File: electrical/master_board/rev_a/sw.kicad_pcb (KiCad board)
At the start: 2 copper layers, 66.2 x 45.2 mm, 7 parts, among them CN108 BRIDGE_SW_OUTER;M1x8

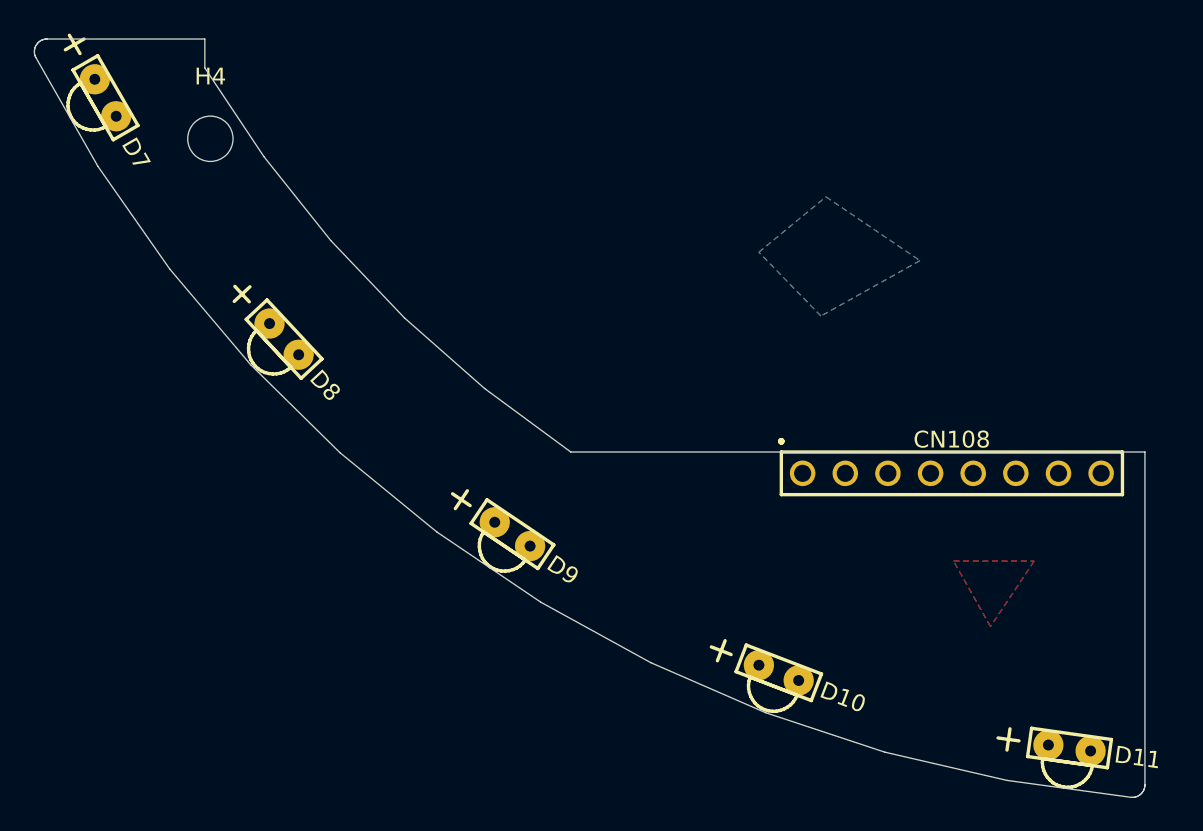
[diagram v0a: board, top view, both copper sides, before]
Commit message: The four corner boards ne/nw/se/sw are now zoned.
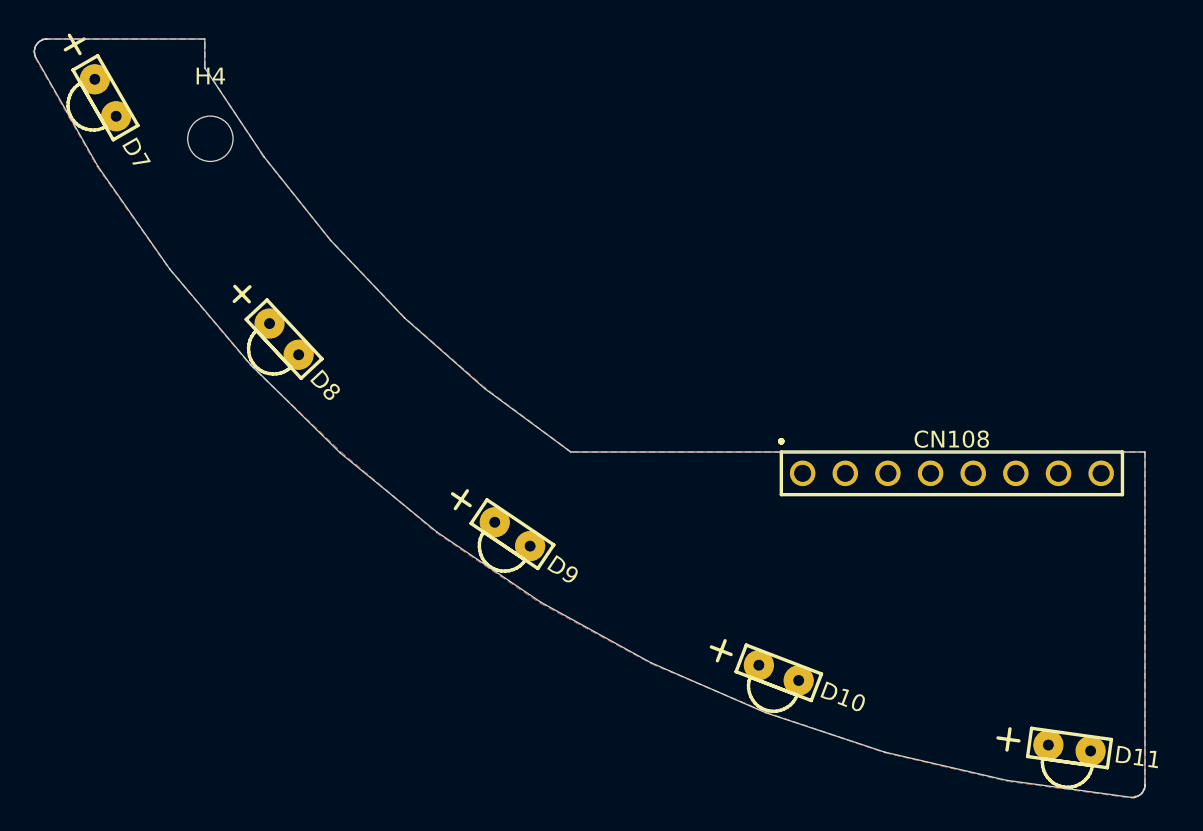
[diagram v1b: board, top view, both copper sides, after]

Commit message: Layed out SW PCB.
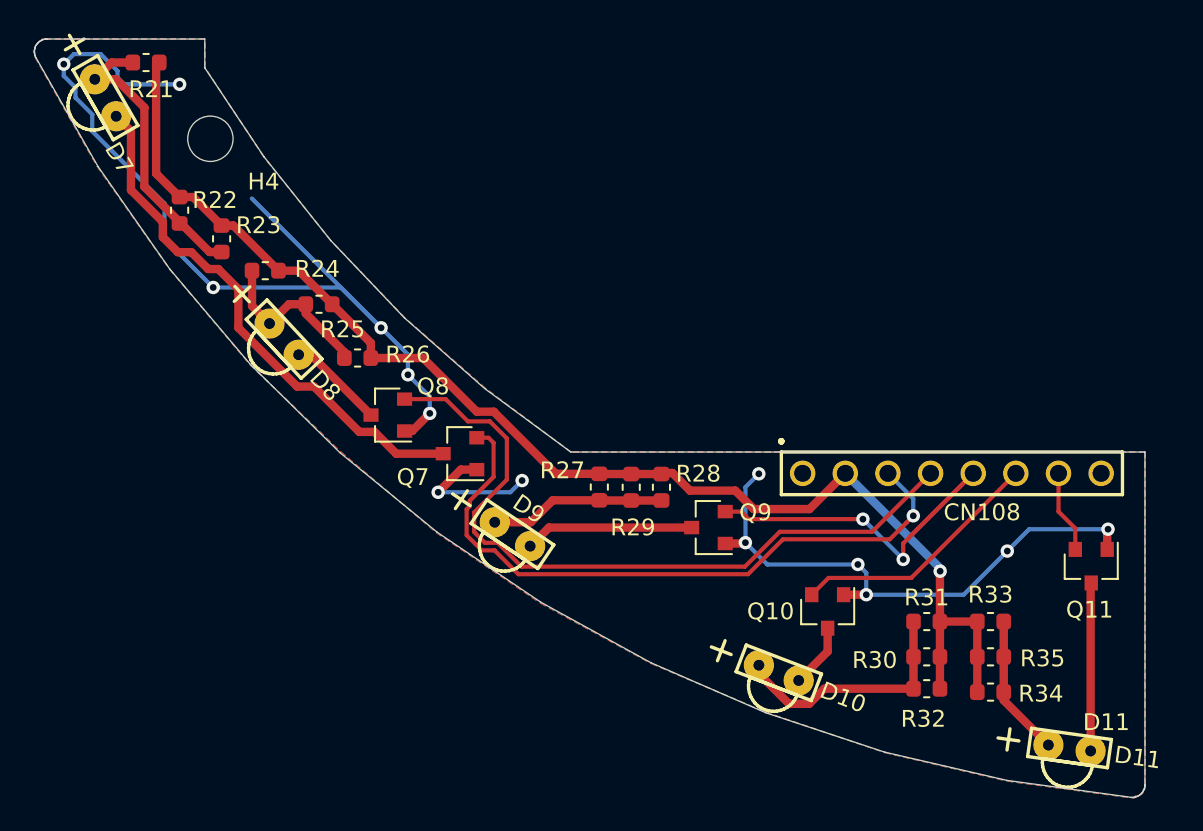
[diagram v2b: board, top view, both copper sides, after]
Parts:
- added Q10: 2N7000;SOT23, Package_TO_SOT_SMD:SOT-23, F.Cu at (74.6, 170.1)
- added Q11: 2N7000;SOT23, Package_TO_SOT_SMD:SOT-23, F.Cu at (90.3, 167.4)
- added Q7: 2N7000;SOT23, Package_TO_SOT_SMD:SOT-23, F.Cu at (52.7, 160.7)
- added Q8: 2N7000;SOT23, Package_TO_SOT_SMD:SOT-23, F.Cu at (48.4, 158.4)
- added Q9: 2N7000;SOT23, Package_TO_SOT_SMD:SOT-23, F.Cu at (67.5, 165.1)
- added R21: 330;1608, Resistor_SMD:R_0603_1608Metric, F.Cu at (34.0, 137.4)
- added R22: 330;1608, Resistor_SMD:R_0603_1608Metric, F.Cu at (36.0, 146.2)
- added R23: 330;1608, Resistor_SMD:R_0603_1608Metric, F.Cu at (38.5, 147.9)
- added R24: 330;1608, Resistor_SMD:R_0603_1608Metric, F.Cu at (41.1, 149.8)
- added R25: 330;1608, Resistor_SMD:R_0603_1608Metric, F.Cu at (44.3, 151.8)
- added R26: 330;1608, Resistor_SMD:R_0603_1608Metric, F.Cu at (46.6, 155.0)
- added R27: 330;1608, Resistor_SMD:R_0603_1608Metric, F.Cu at (61.0, 162.7)
- added R28: 330;1608, Resistor_SMD:R_0603_1608Metric, F.Cu at (64.7, 162.7)
- added R29: 330;1608, Resistor_SMD:R_0603_1608Metric, F.Cu at (62.9, 162.7)
- added R30: 330;1608, Resistor_SMD:R_0603_1608Metric, F.Cu at (80.5, 172.8)
- added R31: 330;1608, Resistor_SMD:R_0603_1608Metric, F.Cu at (80.5, 170.7)
- added R32: 330;1608, Resistor_SMD:R_0603_1608Metric, F.Cu at (80.5, 174.7)
- added R33: 330;1608, Resistor_SMD:R_0603_1608Metric, F.Cu at (84.3, 170.7)
- added R34: 330;1608, Resistor_SMD:R_0603_1608Metric, F.Cu at (84.3, 174.9)
- added R35: 330;1608, Resistor_SMD:R_0603_1608Metric, F.Cu at (84.3, 172.8)
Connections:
- CN108 pad 2: Net-(CN108-Pad2) -> /9V
- CN108 pad 3: Net-(CN108-Pad3) -> /LED7
- CN108 pad 4: Net-(CN108-Pad4) -> /LED8
- CN108 pad 5: Net-(CN108-Pad5) -> /LED9
- CN108 pad 6: Net-(CN108-Pad6) -> /LED10
- CN108 pad 7: Net-(CN108-Pad7) -> /LED11
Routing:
- net /GND: track 0.00 -> 96.9 mm, vias 0 -> 14
- net /9V: track 0.00 -> 79.1 mm, vias 0 -> 1
- net /LED8: track 0.00 -> 43.9 mm
- net /LED7: track 0.00 -> 39.5 mm, vias 0 -> 1
- net Net-(D7-Pad1): track 0.00 -> 31.7 mm
- net /LED9: track 0.00 -> 23.9 mm, vias 0 -> 2
- net Net-(D7-Pad2): track 0.00 -> 17.8 mm
- net /LED10: track 0.00 -> 15.2 mm
- net Net-(D10-Pad2): track 0.00 -> 14.8 mm
- net Net-(D9-Pad2): track 0.00 -> 10.5 mm
- net Net-(D8-Pad2): track 0.00 -> 10.4 mm
- net Net-(D9-Pad1): track 0.00 -> 10.1 mm
- net Net-(D11-Pad1): track 0.00 -> 10.0 mm
- net Net-(D11-Pad2): track 0.00 -> 8.46 mm
- net Net-(D8-Pad1): track 0.00 -> 5.80 mm
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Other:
- board text added: "D11"
